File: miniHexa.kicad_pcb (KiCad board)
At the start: 2 copper layers, 94 x 65.9 mm, 96 parts, among them J2 12v DC, U1 STM32F401RETx, U2 HT7333, U3 RT8289GSP, U4 BQ25886RGE, U5 PCA9685BS, Y1 16Mhz

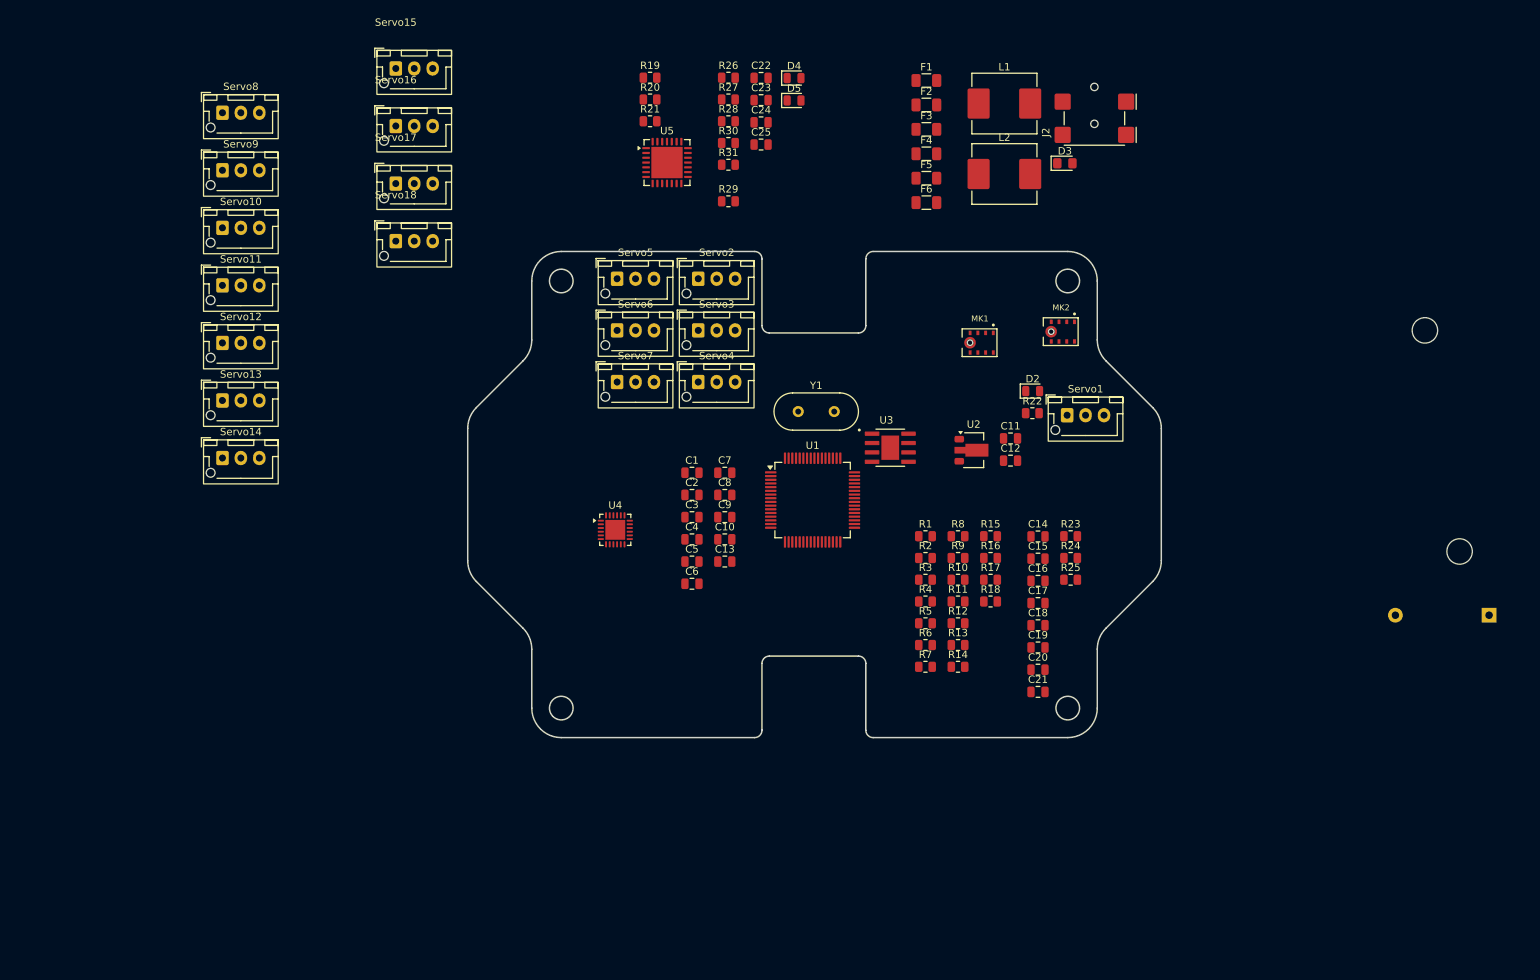
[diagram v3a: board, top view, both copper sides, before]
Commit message: Removed redundent components
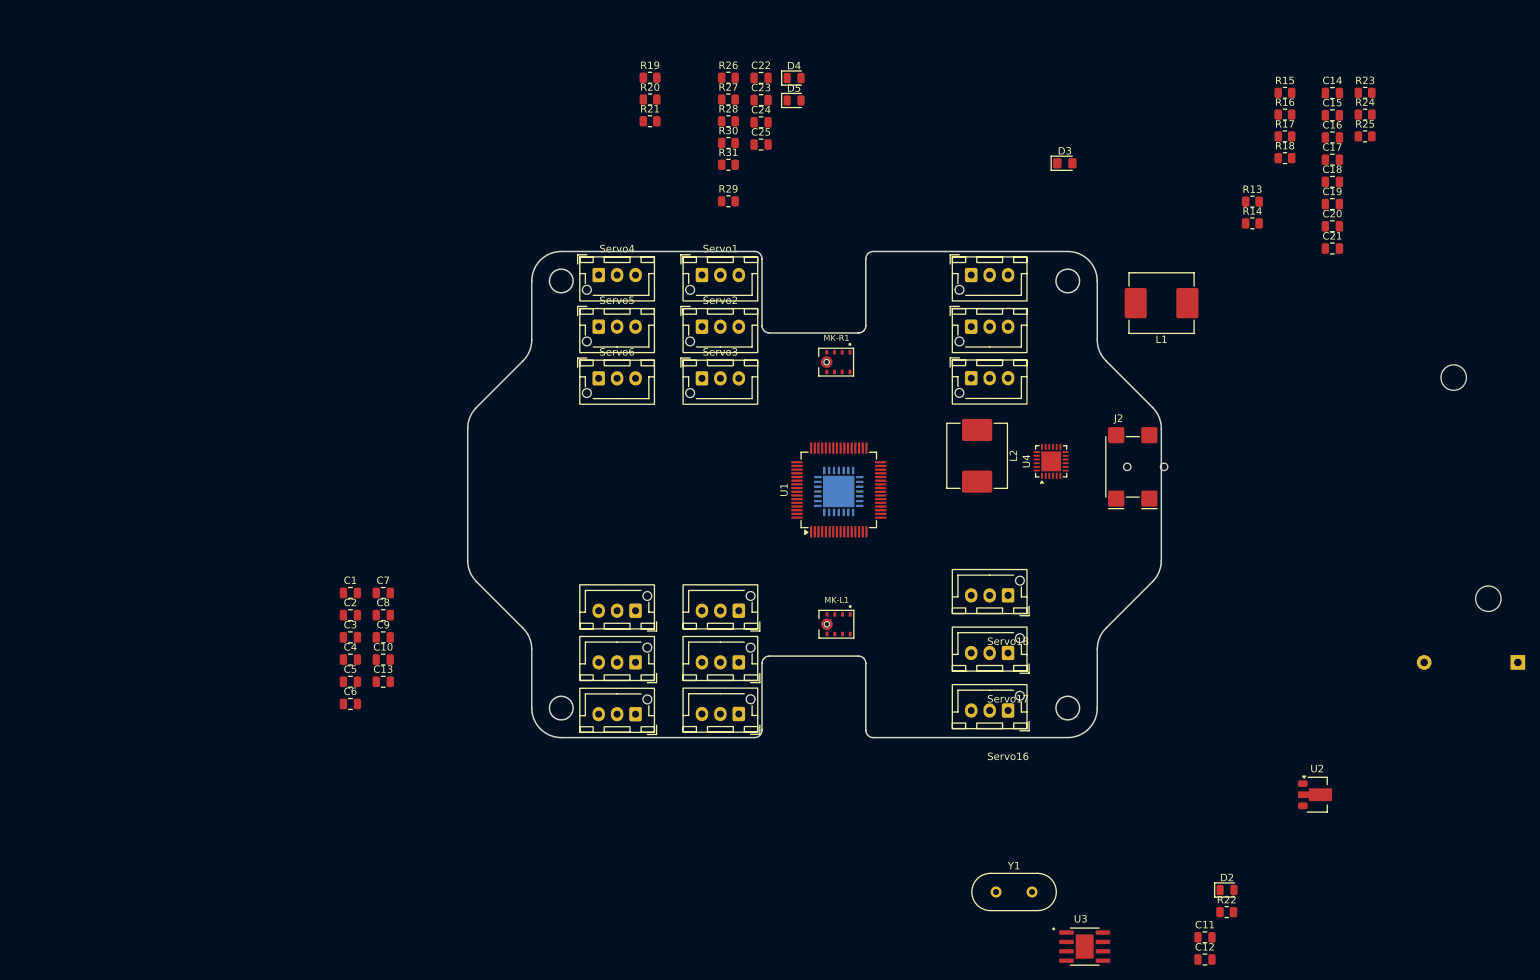
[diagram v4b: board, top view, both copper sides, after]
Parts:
- removed F1, F2, F3, F4, F5, F6: 1A, Fuse:Fuse_1206_3216Metric
- removed R1, R10, R11, R12, R2, R3, R4, R5, R6, R7, R8, R9: 1k, Resistor_SMD:R_0805_2012Metric
- U5: moved to B.Cu
- moved Servo16 114.7 mm to (190.0, 114.0), turned to 180 degrees
- moved Servo17 104.6 mm to (190.0, 106.2), turned to 180 degrees
- moved Servo14 103.0 mm to (185.0, 62.0)
- moved Servo13 102.9 mm to (185.0, 55.0)
- moved Servo8 102.2 mm to (153.5, 107.5), turned to 180 degrees
- moved Servo18 95.9 mm to (190.0, 98.4), turned to 180 degrees
- moved Servo9 92.0 mm to (153.5, 100.5), turned to 180 degrees
- moved Servo15 88.6 mm to (185.0, 69.0)
- moved Servo11 80.7 mm to (139.5, 114.5), turned to 180 degrees
- moved Servo10 76.4 mm to (139.5, 100.5), turned to 180 degrees
- moved C11 72.6 mm to (216.7, 144.8)
- moved C12 72.6 mm to (216.7, 147.8)
- moved R22 72.6 mm to (219.6, 141.3)
- moved U3 72.6 mm to (200.4, 146.0)
- moved D2 72.6 mm to (219.7, 138.4)
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- renumbered MK1 to MK-L1, MK2 to MK-R1
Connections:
- Servo1 pad 1: Net-(Servo1-Pin_1) -> GND
- Servo1 pad 2: VIN -> +5V
- Servo1 pad 3: Net-(Servo1-Pin_3) -> SERVO1
- Servo10 pad 1: Net-(Servo10-Pin_1) -> GND
- Servo10 pad 2: VIN -> +5V
- Servo10 pad 3: Net-(Servo10-Pin_3) -> SERVO10
- Servo11 pad 1: unconnected-(Servo11-Pin_1-Pad1) -> GND
- Servo11 pad 2: VIN -> +5V
- Servo11 pad 3: Net-(Servo11-Pin_3) -> SERVO11
- Servo12 pad 1: unconnected-(Servo12-Pin_1-Pad1) -> GND
- Servo12 pad 2: VIN -> +5V
- Servo12 pad 3: Net-(Servo12-Pin_3) -> SERVO12
- Servo13 pad 1: Net-(Servo13-Pin_1) -> GND
- Servo13 pad 2: VIN -> +5V
- Servo14 pad 1: unconnected-(Servo14-Pin_1-Pad1) -> GND
- Servo14 pad 2: VIN -> +5V
- Servo15 pad 1: unconnected-(Servo15-Pin_1-Pad1) -> GND
- Servo15 pad 2: VIN -> +5V
- Servo16 pad 1: Net-(Servo16-Pin_1) -> GND
- Servo16 pad 2: VIN -> +5V
- Servo17 pad 1: unconnected-(Servo17-Pin_1-Pad1) -> GND
- Servo17 pad 2: VIN -> +5V
- Servo18 pad 1: unconnected-(Servo18-Pin_1-Pad1) -> GND
- Servo18 pad 2: VIN -> +5V
- Servo2 pad 1: unconnected-(Servo2-Pin_1-Pad1) -> GND
- Servo2 pad 2: VIN -> +5V
- Servo2 pad 3: Net-(Servo2-Pin_3) -> SERVO2
- Servo3 pad 1: unconnected-(Servo3-Pin_1-Pad1) -> GND
- Servo3 pad 2: VIN -> +5V
- Servo3 pad 3: Net-(Servo3-Pin_3) -> SERVO3
- Servo4 pad 1: Net-(Servo4-Pin_1) -> GND
- Servo4 pad 2: VIN -> +5V
- Servo4 pad 3: Net-(Servo4-Pin_3) -> SERVO4
- Servo5 pad 1: unconnected-(Servo5-Pin_1-Pad1) -> GND
- Servo5 pad 2: VIN -> +5V
- Servo5 pad 3: Net-(Servo5-Pin_3) -> SERVO5
- Servo6 pad 1: unconnected-(Servo6-Pin_1-Pad1) -> GND
- Servo6 pad 2: VIN -> +5V
- Servo6 pad 3: Net-(Servo6-Pin_3) -> SERVO6
- Servo7 pad 1: Net-(Servo7-Pin_1) -> GND
- Servo7 pad 2: VIN -> +5V
- Servo7 pad 3: Net-(Servo7-Pin_3) -> SERVO7
- Servo8 pad 1: unconnected-(Servo8-Pin_1-Pad1) -> GND
- Servo8 pad 2: VIN -> +5V
- Servo8 pad 3: Net-(Servo8-Pin_3) -> SERVO8
- Servo9 pad 1: unconnected-(Servo9-Pin_1-Pad1) -> GND
- Servo9 pad 2: VIN -> +5V
- Servo9 pad 3: Net-(Servo9-Pin_3) -> SERVO9
